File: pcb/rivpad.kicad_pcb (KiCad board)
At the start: 2 copper layers, 64.2 x 99.3 mm, 39 parts, among them J1 DNP, J2 I2C_Disp, SW1 SW_Push_45deg, SW2 SW_Push_45deg, SW3 SW_Push_45deg, SW4 SW_Push_45deg, SW5 SW_Push_45deg, SW6 SW_Push_45deg, SW7 SW_Push_45deg, SW8 SW_Push_45deg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

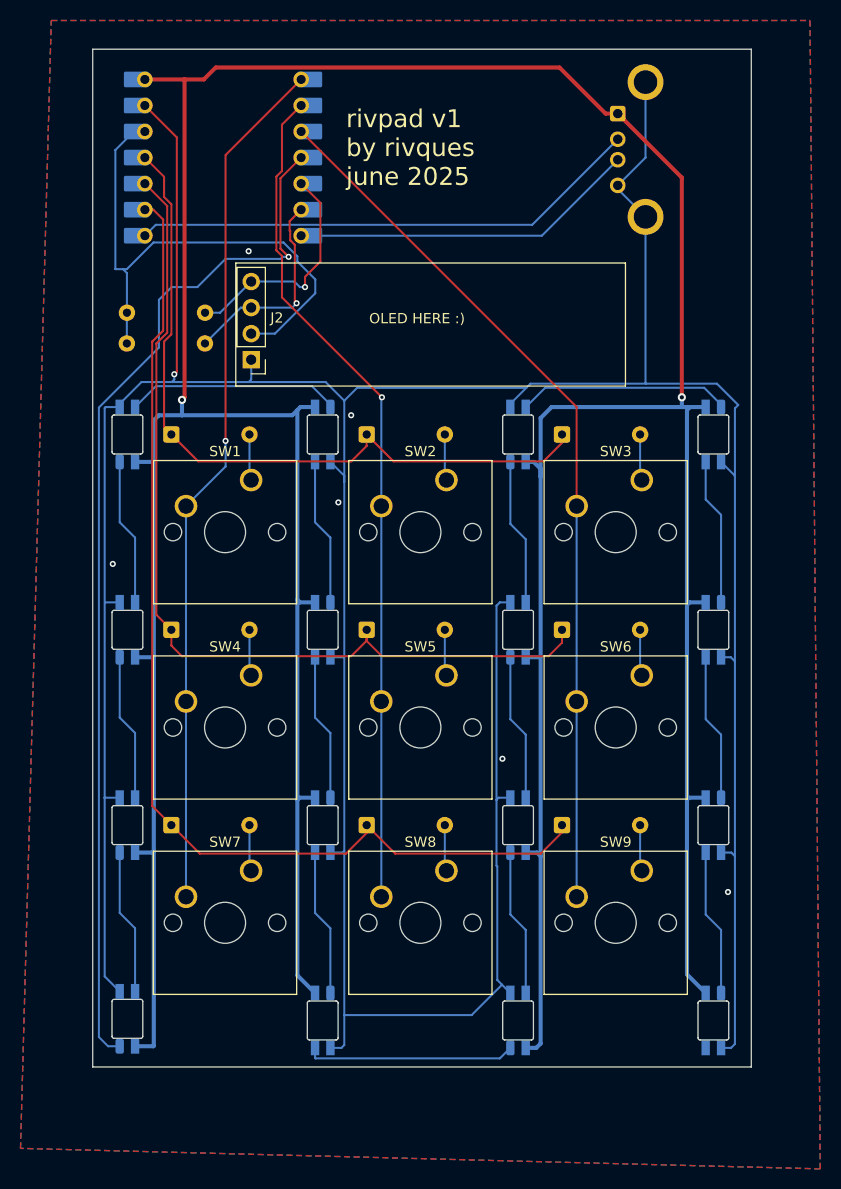
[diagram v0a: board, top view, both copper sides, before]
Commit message: add mounting holes to board and adjust readme
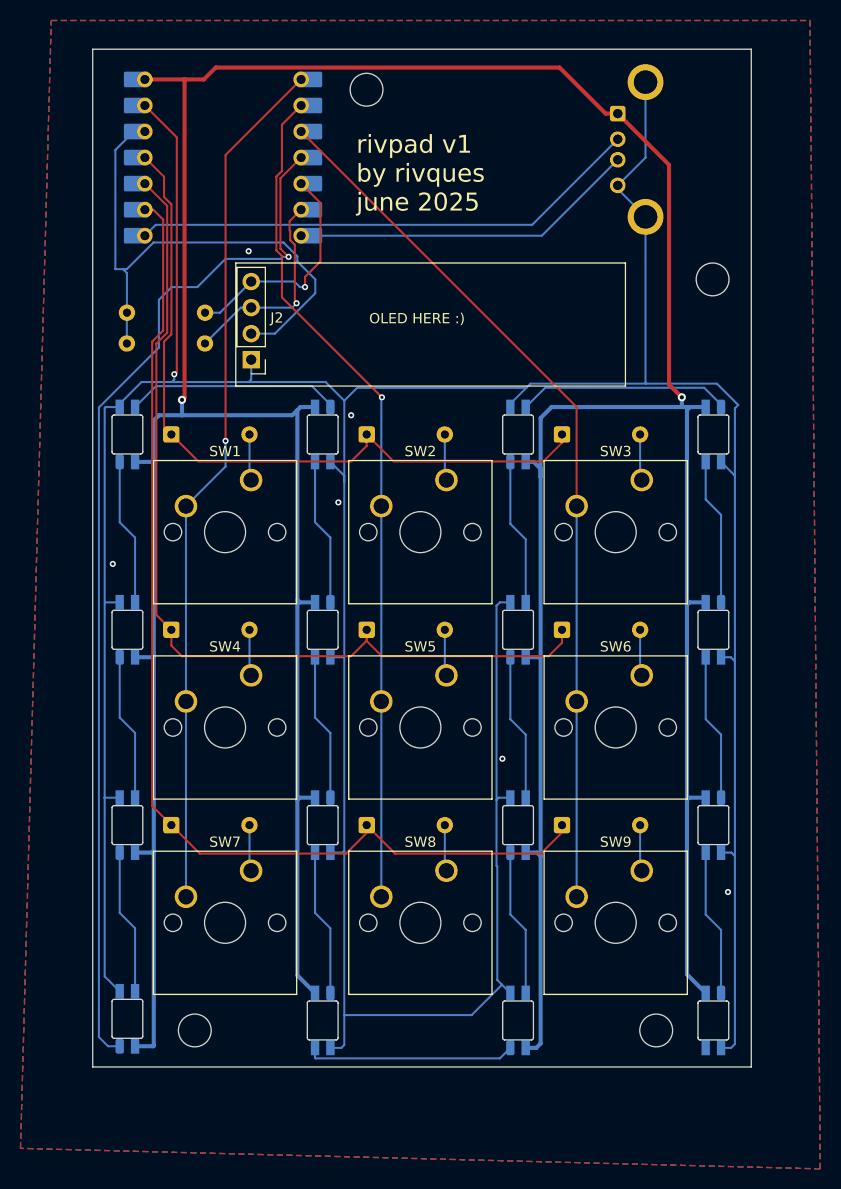
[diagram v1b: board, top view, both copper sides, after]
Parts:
- added REF**: MountingHole_3.2mm_M3, MountingHole:MountingHole_3.2mm_M3, F.Cu at (223.5, 63.2)
- added REF**: MountingHole_3.2mm_M3, MountingHole:MountingHole_3.2mm_M3, F.Cu at (218.0, 136.5)
- added REF**: MountingHole_3.2mm_M3, MountingHole:MountingHole_3.2mm_M3, F.Cu at (189.8, 44.8)
- added REF**: MountingHole_3.2mm_M3, MountingHole:MountingHole_3.2mm_M3, F.Cu at (173.0, 136.5)
